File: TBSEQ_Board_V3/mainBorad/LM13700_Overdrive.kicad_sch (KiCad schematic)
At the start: 35 parts, among them IC1 NJM2125F-TE1, J6 MJ-462, J7 Conn_01x02, U1 LM13700

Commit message: BoardV3
ERCチェック済
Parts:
- removed J7: Conn_01x02, Connector_PinHeader_2.54mm:PinHeader_1x02_P2.54mm_Horizontal, symbol Connector_Generic:Conn_01x02
- added C12: 0.1uF, Capacitor_THT:C_Rect_L7.2mm_W2.5mm_P5.00mm_FKS2_FKP2_MKS2_MKP2, symbol Device:C_Small
- added C20: 1uF/50V, Capacitor_THT:CP_Radial_D5.0mm_P2.00mm, symbol Device:C_Polarized_Small
- added C21: 0.033uF, Capacitor_THT:C_Rect_L7.2mm_W2.5mm_P5.00mm_FKS2_FKP2_MKS2_MKP2, symbol Device:C_Small
- added D1, D2, D3: D, Diode_THT:D_A-405_P2.54mm_Vertical_AnodeUp, symbol Device:D
- added J12: Conn_01x02, Connector_PinHeader_2.54mm:PinHeader_1x02_P2.54mm_Vertical, symbol Connector_Generic:Conn_01x02
- added Q1: NPN, Package_TO_SOT_THT:TO-92_Inline, symbol Device:Q_NPN_ECB
- added Q2: PNP, Package_TO_SOT_THT:TO-92_Inline, symbol Device:Q_PNP_ECB
- added R21, R30: 22K, Resistor_THT:R_Axial_DIN0207_L6.3mm_D2.5mm_P2.54mm_Vertical, symbol Device:R
- added R22, R25: 100, Resistor_THT:R_Axial_DIN0207_L6.3mm_D2.5mm_P2.54mm_Vertical, symbol Device:R
- added R26: 2.2K, Resistor_THT:R_Axial_DIN0207_L6.3mm_D2.5mm_P2.54mm_Vertical, symbol Device:R
- added R27: 1.5M, Resistor_THT:R_Axial_DIN0207_L6.3mm_D2.5mm_P2.54mm_Vertical, symbol Device:R
- added R28: 220K, Resistor_THT:R_Axial_DIN0207_L6.3mm_D2.5mm_P2.54mm_Vertical, symbol Device:R
- added R29, VCA_R1: 47K, Resistor_THT:R_Axial_DIN0207_L6.3mm_D2.5mm_P2.54mm_Vertical, symbol Device:R
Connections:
- net A+12V: now also R27.1
- net GNDA: now also C12.1, C20.2, C21.1, J12.2 (Pin_2), R22.2
- net at J6.T1, J6.TS1, VR9.2 (WIPER): now also J12.1 (Pin_1)
- net +5.333VA renamed A+5.333V
- net A+_VCA_Control renamed A+VCA_Control
- net A+VCA_Control: now also VCA_R1.1
- net A+_VCA_Resonance renamed A+VCA_Resonance
- net A+_VCA_Signal renamed A+VCA_Signal
- new net: R26.1, R28.2
- new net: D2.1 (K), R26.2
- new net: Q2.1 (E), R28.1
- new net: C21.2, R29.1, R30.2
- new net: D3.1 (K), Q2.2 (C), VCA_R1.2
- new net: C20.1, Q2.3 (B), R25.1, R27.2
- new net: C12.2, Q1.3 (B), R21.1
- new net: D1.1 (K), R21.2
- new net: D3.2 (A), R30.1
- new net: Q1.2 (C), R25.2
- new net: Q1.1 (E), R22.1
- new net A+VCA-Reso_ACC: R29.2
- new net A+VCA_Env: D1.2 (A)
- new net A+VCA_Trig: D2.2 (A)
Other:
- moved on the sheet: C4, C9, R10, R11, R12, R13, R14, R9, TM1, U1C, U1D, U1E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

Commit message: V3Board
opamp Dip8に対応
部品配置
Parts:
- removed IC1: NJM2125F-TE1, SamacSys_Parts:SOT95P280X130-5N, symbol SamacSys_Parts:NJM2125F-TE1
- added IC1: NJM2125F-TE1_DIP8, SamacSys_Parts:NJM2125F-SOT95&DIP8, symbol SamacSys_Parts:NJM2125F-TE1_DIP-8
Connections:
- net A+12V: now also IC1.8 (V+)
- net GNDA: now also IC1.4 (GND)
- net at C5.1, R15.2, R23.2: now also IC1.3 (+INPUT)
- net at R17.1, R24.2: now also IC1.1 (OUTPUT)
- net at R16.2, R24.1: now also IC1.2 (-INPUT)
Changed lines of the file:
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@@
 	(wire
 		(pts
-			(xy 135.89 149.86) (xy 135.89 158.75)
+			(xy 135.89 149.86) (xy 135.89 172.72)
 		)
 		(stroke
@@
 	(wire
 		(pts
-			(xy 135.89 158.75) (xy 133.35 158.75)
+			(xy 135.89 172.72) (xy 133.35 172.72)
 		)
 		(stroke
@@
 	(global_label "A+12V"
 		(shape input)
-		(at 133.35 158.75 180)
+		(at 133.35 172.72 180)
 		(fields_autoplaced yes)
 		(effects
@@
 		)
 		(property "Intersheetrefs" "${INTERSHEET_REFS}"
-			(at 121.1724 158.75 0)
+			(at 121.1724 172.72 0)
 			(effects
 				(font
@@
 	)
 	(symbol
+		(lib_id "SamacSys_Parts:NJM2125F-TE1_DIP-8")
+		(at 101.6 147.32 0)
+		(unit 1)
+		(exclude_from_sim no)
+		(in_bom yes)
+		(on_board yes)
+		(dnp no)
+		(fields_autoplaced yes)
+		(property "Reference" "IC1"
+			(at 118.11 139.7 0)
+			(effects
+				(font
+					(size 1.27 1.27)
+				)
+			)
+		)
+		(property "Value" "NJM2125F-TE1_DIP8"
+			(at 118.11 142.24 0)
+			(effects
+				(font
+					(size 1.27 1.27)
+				)
+			)
+		)
+		(property "Footprint" "SamacSys_Parts:NJM2125F-SOT95&DIP8"
+			(at 130.81 242.24 0)
+			(effects
+				(font
+					(size 1.27 1.27)
+				)
+				(justify left top)
+				(hide yes)
+			)
+		)
+		(property "Datasheet" "https://componentsearchengine.com/Datasheets/1/NJM2125F-TE1.pdf"
+			(at 130.81 342.24 0)
+			(effects
+				(font
+					(size 1.27 1.27)
+				)
+				(justify left top)
+				(hide yes)
+			)
+		)
+		(property "Description" "Operational Amplifiers - Op Amps Single Supply"
+			(at 101.6 147.32 0)
+			(effects
+				(font
+					(size 1.27 1.27)
+				)
+				(hide yes)
+			)
+		)
+		(property "Height" "1.3"
+			(at 130.81 542.24 0)
+			(effects
+				(font
+					(size 1.27 1.27)
+				)
+				(justify left top)
+				(hide yes)
+			)
+		)
+		(property "Manufacturer_Name" "New Japan Radio"
+			(at 130.81 642.24 0)
+			(effects
+				(font
+					(size 1.27 1.27)
+				)
+				(justify left top)
+				(hide yes)
+			)
+		)
+		(property "Manufacturer_Part_Number" "NJM2125F-TE1"
+			(at 130.81 742.24 0)
+			(effects
+				(font
+					(size 1.27 1.27)
+				)
+				(justify left top)
+				(hide yes)
+			)
+		)
+		(property "Mouser Part Number" "513-NJM2125F-TE1"
+			(at 130.81 842.24 0)
+			(effects
+				(font
+					(size 1.27 1.27)
+				)
+				(justify left top)
+				(hide yes)
+			)
+		)
+		(property "Mouser Price/Stock" "https://www.mouser.co.uk/ProductDetail/NJR/NJM2125F-TE1?qs=SzzEZJ0VecQ3YU3q3zUUYw%3D%3D"
+			(at 130.81 942.24 0)
+			(effects
+				(font
+					(size 1.27 1.27)
+				)
+				(justify left top)
+				(hide yes)
+			)
+		)
+		(property "Arrow Part Number" ""
+			(at 130.81 1042.24 0)
+			(effects
+				(font
+					(size 1.27 1.27)
+				)
+				(justify left top)
+				(hide yes)
+			)
+		)
+		(property "Arrow Price/Stock" ""
+			(at 130.81 1142.24 0)
+			(effects
+				(font
+					(size 1.27 1.27)
+				)
+				(justify left top)
+				(hide yes)
+			)
+		)
+		(pin "4"
+		)
+		(pin "7"
+		)
+		(pin "1"
+		)
+		(pin "3"
+		)
+		(pin "8"
+		)
+		(pin "5"
+		)
+		(pin "6"
+		)
+		(pin "2"
+		)
+		(instances
+			(project ""
+				(path "/83af791a-9776-40a7-82ad-9528ff7474b8/60eab4e1-ce34-4d77-8d9b-d611705cbf82"
+					(reference "IC1")
+					(unit 1)
+				)
+			)
+		)
+	)
+	(symbol
 		(lib_id "Device:R")
 		(at 257.81 67.31 270)
@@
 					(unit 1)
 				)
-			)
-		)
-	)
-	(symbol
-		(lib_id "SamacSys_Parts:NJM2125F-TE1")
-		(at 101.6 147.32 0)
-		(unit 1)
-		(exclude_from_sim no)
-		(in_bom yes)
-		(on_board yes)
-		(dnp no)
-		(fields_autoplaced yes)
-		(property "Reference" "IC1"
-			(at 118.11 139.7 0)
-			(effects
-				(font
-					(size 1.27 1.27)
-				)
-			)
-		)
-		(property "Value" "NJM2125F-TE1"
-			(at 118.11 142.24 0)
-			(effects
-				(font
-					(size 1.27 1.27)
-				)
-			)
-		)
-		(property "Footprint" "SamacSys_Parts:SOT95P280X130-5N"
-			(at 130.81 242.24 0)
-			(effects
-				(font
-					(size 1.27 1.27)
-				)
-				(justify left top)
-				(hide yes)
-			)
-		)
-		(property "Datasheet" "https://componentsearchengine.com/Datasheets/1/NJM2125F-TE1.pdf"
-			(at 130.81 342.24 0)
-			(effects
-				(font
-					(size 1.27 1.27)
-				)
-				(justify left top)
-				(hide yes)
-			)
-		)
-		(property "Description" "Operational Amplifiers - Op Amps Single Supply"
-			(at 101.6 147.32 0)
-			(effects
-				(font
-					(size 1.27 1.27)
-				)
-				(hide yes)
-			)
-		)
-		(property "Height" "1.3"
-			(at 130.81 542.24 0)
-			(effects
-				(font
-					(size 1.27 1.27)
-				)
-				(justify left top)
-				(hide yes)
-			)
-		)
-		(property "Manufacturer_Name" "New Japan Radio"
-			(at 130.81 642.24 0)
-			(effects
-				(font
-					(size 1.27 1.27)
-				)
-				(justify left top)
-				(hide yes)
-			)
-		)
-		(property "Manufacturer_Part_Number" "NJM2125F-TE1"
-			(at 130.81 742.24 0)
-			(effects
-				(font
-					(size 1.27 1.27)
-				)
-				(justify left top)
-				(hide yes)
-			)
-		)
-		(property "Mouser Part Number" "513-NJM2125F-TE1"
-			(at 130.81 842.24 0)
-			(effects
-				(font
-					(size 1.27 1.27)
-				)
-				(justify left top)
-				(hide yes)
-			)
-		)
-		(property "Mouser Price/Stock" "https://www.mouser.co.uk/ProductDetail/NJR/NJM2125F-TE1?qs=SzzEZJ0VecQ3YU3q3zUUYw%3D%3D"
-			(at 130.81 942.24 0)
-			(effects
-				(font
-					(size 1.27 1.27)
-				)
-				(justify left top)
-				(hide yes)
-			)
-		)
-		(property "Arrow Part Number" ""
-			(at 130.81 1042.24 0)
-			(effects
-				(font
-					(size 1.27 1.27)
-				)
-				(justify left top)
-				(hide yes)
-			)
-		)
-		(property "Arrow Price/Stock" ""
-			(at 130.81 1142.24 0)
-			(effects
-				(font
-					(size 1.27 1.27)
-				)
-				(justify left top)
-				(hide yes)
-			)
-		)
-		(pin "5"
-		)
-		(pin "3"
-		)
-		(pin "2"
-		)
-		(pin "1"
-		)
-		(pin "4"
-		)
-		(instances
-			(project ""
-				(path "/83af791a-9776-40a7-82ad-9528ff7474b8/60eab4e1-ce34-4d77-8d9b-d611705cbf82"
-					(reference "IC1")
-					(unit 1)
-				)

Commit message: V3Board
アートワーク仮配置
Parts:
- Q1, Q2: footprint Package_TO_SOT_THT:TO-92_Inline -> Package_TO_SOT_THT:TO-92_HandSolder
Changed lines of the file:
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@@
 			)
 		)
-		(property "Footprint" "Package_TO_SOT_THT:TO-92_Inline"
+		(property "Footprint" "Package_TO_SOT_THT:TO-92_HandSolder"
 			(at 246.38 62.23 0)
 			(effects
@@
 			)
 		)
-		(property "Footprint" "Package_TO_SOT_THT:TO-92_Inline"
+		(property "Footprint" "Package_TO_SOT_THT:TO-92_HandSolder"
 			(at 208.28 55.88 0)
 			(effects

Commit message: V3Board
スペーサー穴追加
オートルーター後
DualTr,OPアンプは表面実装に切り替え
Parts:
- removed IC1: NJM2125F-TE1_DIP8, SamacSys_Parts:NJM2125F-SOT95&DIP8, symbol SamacSys_Parts:NJM2125F-TE1_DIP-8
- added IC1: NJM2125F-TE1, SamacSys_Parts:SOT95P280X130-5N, symbol SamacSys_Parts:NJM2125F-TE1
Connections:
- net A+12V: now also IC1.5 (V+)
- net GNDA: now also IC1.2 (GND)
- net at C5.1, R15.2, R23.2: now also IC1.1 (+INPUT)
- net at R17.1, R24.2: now also IC1.4 (OUTPUT)
- net at R16.2, R24.1: now also IC1.3 (-INPUT)
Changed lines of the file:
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@@
+	)
+	(symbol
+		(lib_id "SamacSys_Parts:NJM2125F-TE1")
+		(at 101.6 147.32 0)
+		(unit 1)
+		(exclude_from_sim no)
+		(in_bom yes)
+		(on_board yes)
+		(dnp no)
+		(fields_autoplaced yes)
+		(property "Reference" "IC1"
+			(at 118.11 139.7 0)
+			(effects
+				(font
+					(size 1.27 1.27)
+				)
+			)
+		)
+		(property "Value" "NJM2125F-TE1"
+			(at 118.11 142.24 0)
+			(effects
+				(font
+					(size 1.27 1.27)
+				)
+			)
+		)
+		(property "Footprint" "SamacSys_Parts:SOT95P280X130-5N"
+			(at 130.81 242.24 0)
+			(effects
+				(font
+					(size 1.27 1.27)
+				)
+				(justify left top)
+				(hide yes)
+			)
+		)
+		(property "Datasheet" "https://componentsearchengine.com/Datasheets/1/NJM2125F-TE1.pdf"
+			(at 130.81 342.24 0)
+			(effects
+				(font
+					(size 1.27 1.27)
+				)
+				(justify left top)
+				(hide yes)
+			)
+		)
+		(property "Description" "Operational Amplifiers - Op Amps Single Supply"
+			(at 101.6 147.32 0)
+			(effects
+				(font
+					(size 1.27 1.27)
+				)
+				(hide yes)
+			)
+		)
+		(property "Height" "1.3"
+			(at 130.81 542.24 0)
+			(effects
+				(font
+					(size 1.27 1.27)
+				)
+				(justify left top)
+				(hide yes)
+			)
+		)
+		(property "Manufacturer_Name" "New Japan Radio"
+			(at 130.81 642.24 0)
+			(effects
+				(font
+					(size 1.27 1.27)
+				)
+				(justify left top)
+				(hide yes)
+			)
+		)
+		(property "Manufacturer_Part_Number" "NJM2125F-TE1"
+			(at 130.81 742.24 0)
+			(effects
+				(font
+					(size 1.27 1.27)
+				)
+				(justify left top)
+				(hide yes)
+			)
+		)
+		(property "Mouser Part Number" "513-NJM2125F-TE1"
+			(at 130.81 842.24 0)
+			(effects
+				(font
+					(size 1.27 1.27)
+				)
+				(justify left top)
+				(hide yes)
+			)
+		)
+		(property "Mouser Price/Stock" "https://www.mouser.co.uk/ProductDetail/NJR/NJM2125F-TE1?qs=SzzEZJ0VecQ3YU3q3zUUYw%3D%3D"
+			(at 130.81 942.24 0)
+			(effects
+				(font
+					(size 1.27 1.27)
+				)
+				(justify left top)
+				(hide yes)
+			)
+		)
+		(property "Arrow Part Number" ""
+			(at 130.81 1042.24 0)
+			(effects
+				(font
+					(size 1.27 1.27)
+				)
+				(justify left top)
+				(hide yes)
+			)
+		)
+		(property "Arrow Price/Stock" ""
+			(at 130.81 1142.24 0)
+			(effects
+				(font
+					(size 1.27 1.27)
+				)
+				(justify left top)
+				(hide yes)
+			)
+		)
+		(pin "2"
+		)
+		(pin "4"
+		)
+		(pin "5"
+		)
+		(pin "3"
+		)
+		(pin "1"
+		)
+		(instances
+			(project ""
+				(path "/83af791a-9776-40a7-82ad-9528ff7474b8/60eab4e1-ce34-4d77-8d9b-d611705cbf82"
+					(reference "IC1")
+					(unit 1)
+				)
+			)
+		)
 	)
 	(symbol
@@
 					(unit 1)
 				)
-			)
-		)
-	)
-	(symbol
-		(lib_id "SamacSys_Parts:NJM2125F-TE1_DIP-8")
-		(at 101.6 147.32 0)
-		(unit 1)
-		(exclude_from_sim no)
-		(in_bom yes)
-		(on_board yes)
-		(dnp no)
-		(fields_autoplaced yes)
-		(property "Reference" "IC1"
-			(at 118.11 139.7 0)
-			(effects
-				(font
-					(size 1.27 1.27)
-				)
-			)
-		)
-		(property "Value" "NJM2125F-TE1_DIP8"
-			(at 118.11 142.24 0)
-			(effects
-				(font
-					(size 1.27 1.27)
-				)
-			)
-		)
-		(property "Footprint" "SamacSys_Parts:NJM2125F-SOT95&DIP8"
-			(at 130.81 242.24 0)
-			(effects
-				(font
-					(size 1.27 1.27)
-				)
-				(justify left top)
-				(hide yes)
-			)
-		)
-		(property "Datasheet" "https://componentsearchengine.com/Datasheets/1/NJM2125F-TE1.pdf"
-			(at 130.81 342.24 0)
-			(effects
-				(font
-					(size 1.27 1.27)
-				)
-				(justify left top)
-				(hide yes)
-			)
-		)
-		(property "Description" "Operational Amplifiers - Op Amps Single Supply"
-			(at 101.6 147.32 0)
-			(effects
-				(font
-					(size 1.27 1.27)
-				)
-				(hide yes)
-			)
-		)
-		(property "Height" "1.3"
-			(at 130.81 542.24 0)
-			(effects
-				(font
-					(size 1.27 1.27)
-				)
-				(justify left top)
-				(hide yes)
-			)
-		)
-		(property "Manufacturer_Name" "New Japan Radio"
-			(at 130.81 642.24 0)
-			(effects
-				(font
-					(size 1.27 1.27)
-				)
-				(justify left top)
-				(hide yes)
-			)
-		)
-		(property "Manufacturer_Part_Number" "NJM2125F-TE1"
-			(at 130.81 742.24 0)
-			(effects
-				(font
-					(size 1.27 1.27)
-				)
-				(justify left top)
-				(hide yes)
-			)
-		)
-		(property "Mouser Part Number" "513-NJM2125F-TE1"
-			(at 130.81 842.24 0)
-			(effects
-				(font
-					(size 1.27 1.27)
-				)
-				(justify left top)
-				(hide yes)
-			)
-		)
-		(property "Mouser Price/Stock" "https://www.mouser.co.uk/ProductDetail/NJR/NJM2125F-TE1?qs=SzzEZJ0VecQ3YU3q3zUUYw%3D%3D"
-			(at 130.81 942.24 0)
-			(effects
-				(font
-					(size 1.27 1.27)
-				)
-				(justify left top)
-				(hide yes)
-			)
-		)
-		(property "Arrow Part Number" ""
-			(at 130.81 1042.24 0)
-			(effects
-				(font
-					(size 1.27 1.27)
-				)
-				(justify left top)
-				(hide yes)
-			)
-		)
-		(property "Arrow Price/Stock" ""
-			(at 130.81 1142.24 0)
-			(effects
-				(font
-					(size 1.27 1.27)
-				)
-				(justify left top)
-				(hide yes)
-			)
-		)
-		(property "Sim.Library" ""
-			(at 101.6 147.32 0)
-			(effects
-				(font
-					(size 1.27 1.27)
-				)
-				(hide yes)
-			)
-		)
-		(property "Sim.Name" ""
-			(at 101.6 147.32 0)
-			(effects
-				(font
-					(size 1.27 1.27)
-				)
-				(hide yes)
-			)
-		)
-		(pin "4"
-		)
-		(pin "7"
-		)
-		(pin "1"
-		)
-		(pin "3"
-		)
-		(pin "8"
-		)
-		(pin "5"
-		)
-		(pin "6"
-		)
-		(pin "2"
-		)
-		(instances
-			(project ""
-				(path "/83af791a-9776-40a7-82ad-9528ff7474b8/60eab4e1-ce34-4d77-8d9b-d611705cbf82"
-					(reference "IC1")
-					(unit 1)
-				)

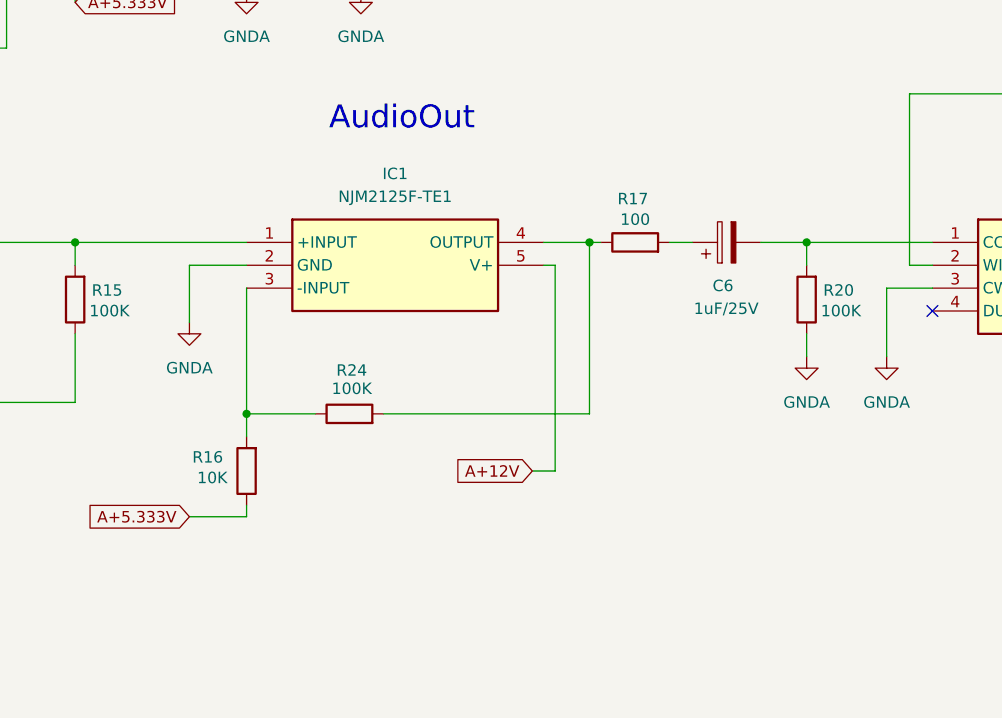
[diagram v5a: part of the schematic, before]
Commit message: V3Board
DualTr OPAmp やはりDIPに変更してオートルーター前に戻す
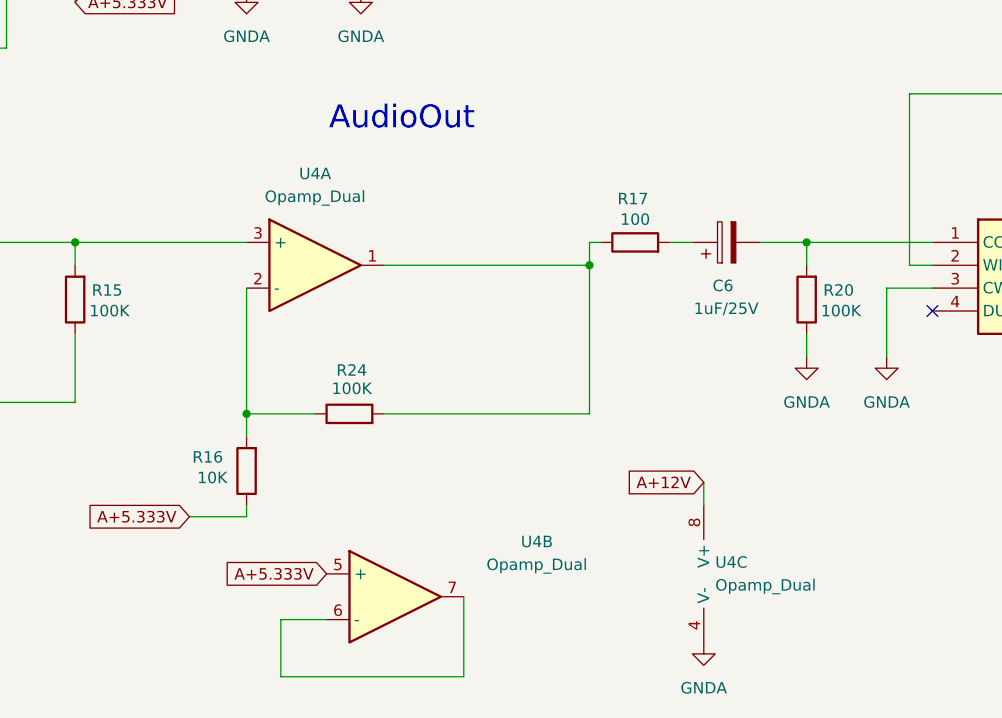
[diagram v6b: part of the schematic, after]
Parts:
- removed IC1: NJM2125F-TE1, SamacSys_Parts:SOT95P280X130-5N, symbol SamacSys_Parts:NJM2125F-TE1
- added U4: Opamp_Dual, Package_DIP:DIP-8_W7.62mm_LongPads, symbol Device:Opamp_Dual
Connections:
- net A+12V: now also U4.8 (V+)
- net A+5.333V: now also U4.5 (+)
- net GNDA: now also U4.4 (V-)
- net at C5.1, R15.2, R23.2: now also U4.3 (+)
- net at R16.2, R24.1: now also U4.2 (-)
- net at R17.1, R24.2: now also U4.1
- new net: U4.6 (-), U4.7
